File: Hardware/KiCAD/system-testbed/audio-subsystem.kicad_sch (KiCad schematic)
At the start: 29 parts, among them J1 Conn_02x13_Odd_Even, SW1 SW_SPDT, U2 MAX98357A

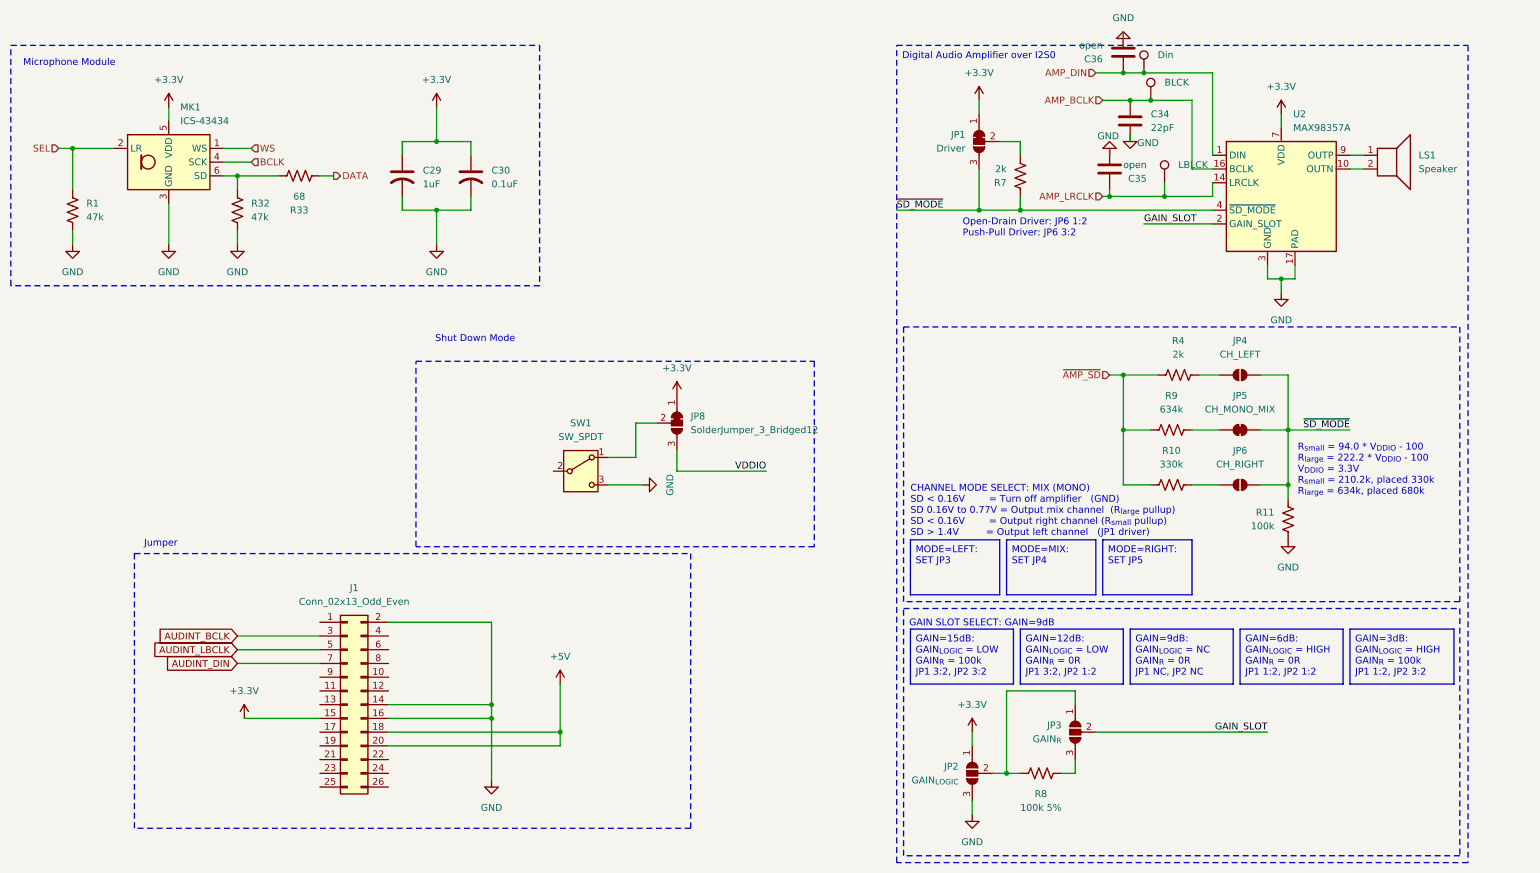
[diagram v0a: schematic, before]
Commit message: feat: capture Audio PCB #32 feat: begin I2S Pin Mapping and Interconnects #53
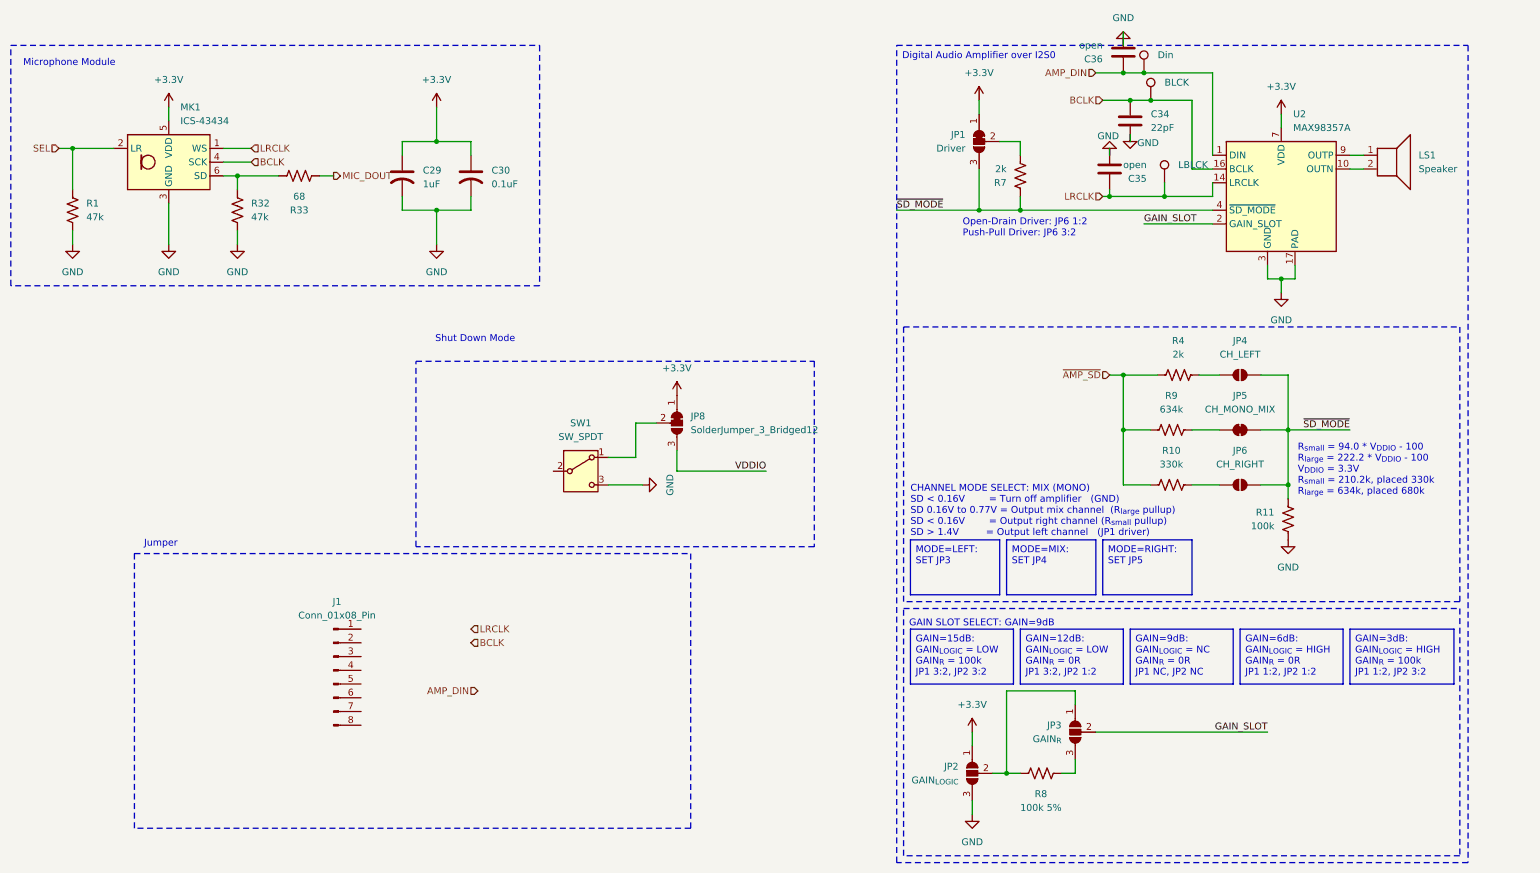
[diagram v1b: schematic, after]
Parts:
- J1: value Conn_02x13_Odd_Even -> Conn_01x08_Pin; symbol Connector_Generic:Conn_02x13_Odd_Even -> Connector:Conn_01x08_Pin
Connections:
- net AMP_BCLK is gone; now on net BCLK: BLCK.1, C34.1, U2.16 (BCLK)
- net WS is gone; now on net LRCLK: MK1.1 (WS)
- net +3.3V: no longer J1.15 (Pin_15)
- net GND: no longer J1.14 (Pin_14), J1.16 (Pin_16), J1.2 (Pin_2)
- removed net +5V: J1.18 (Pin_18), J1.20 (Pin_20)
- net AMP_LRCLK renamed LRCLK
- net AUDINT_BCLK: no longer names the net of J1.3 (Pin_3)
- net AUDINT_DIN: no longer names the net of J1.7 (Pin_7)
- net AUDINT_LBCLK: no longer names the net of J1.5 (Pin_5)
- net DATA renamed MIC_DOUT

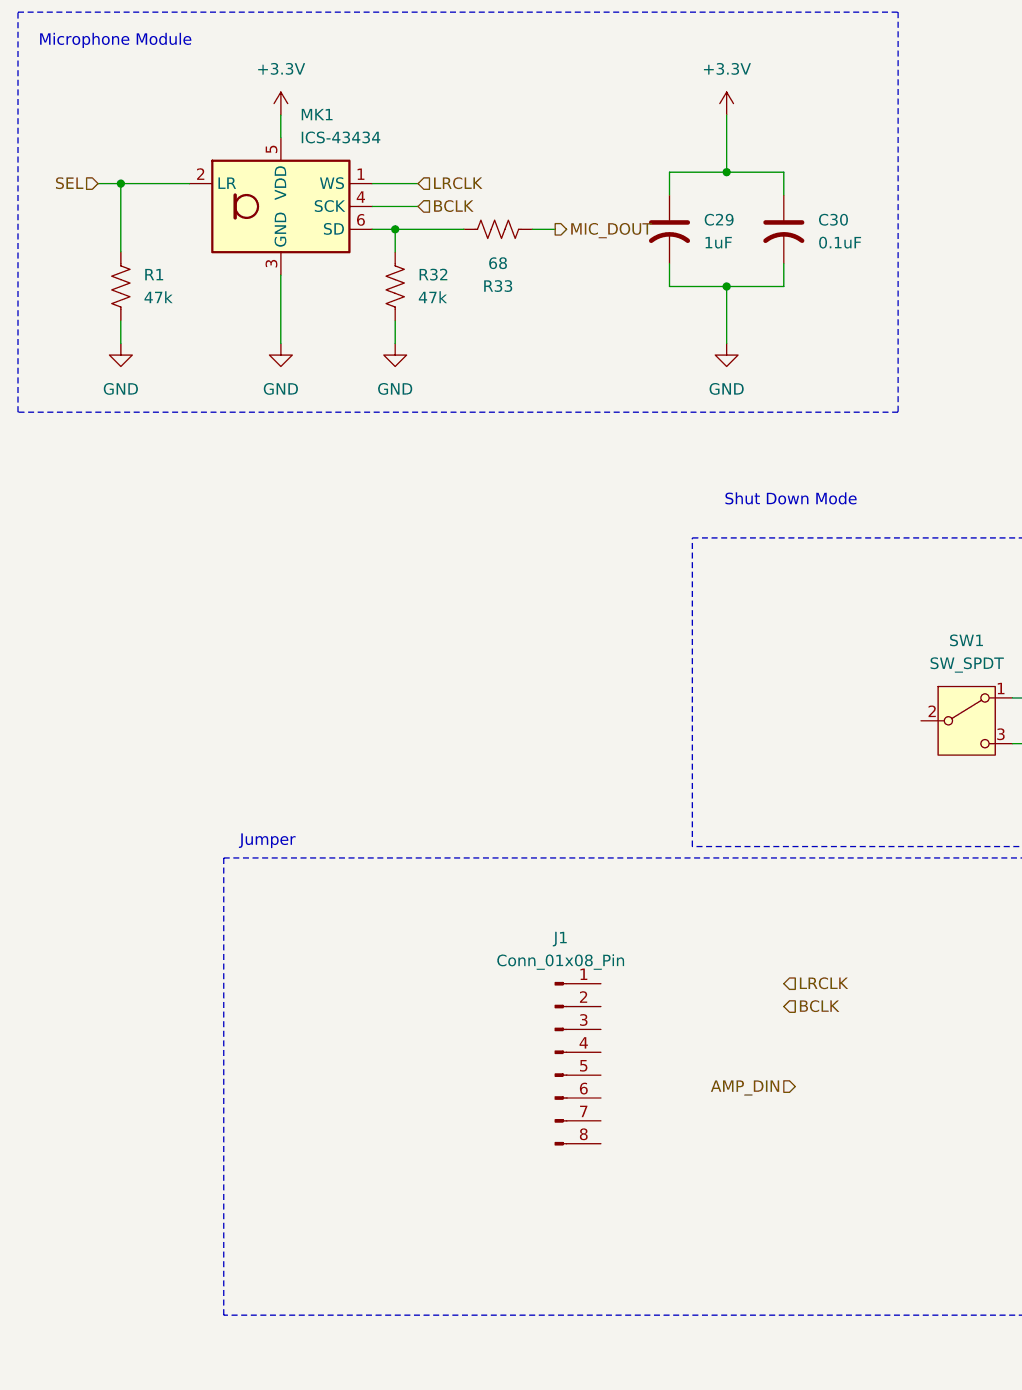
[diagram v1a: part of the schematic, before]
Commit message: fix: clarify labellng and pin head #32
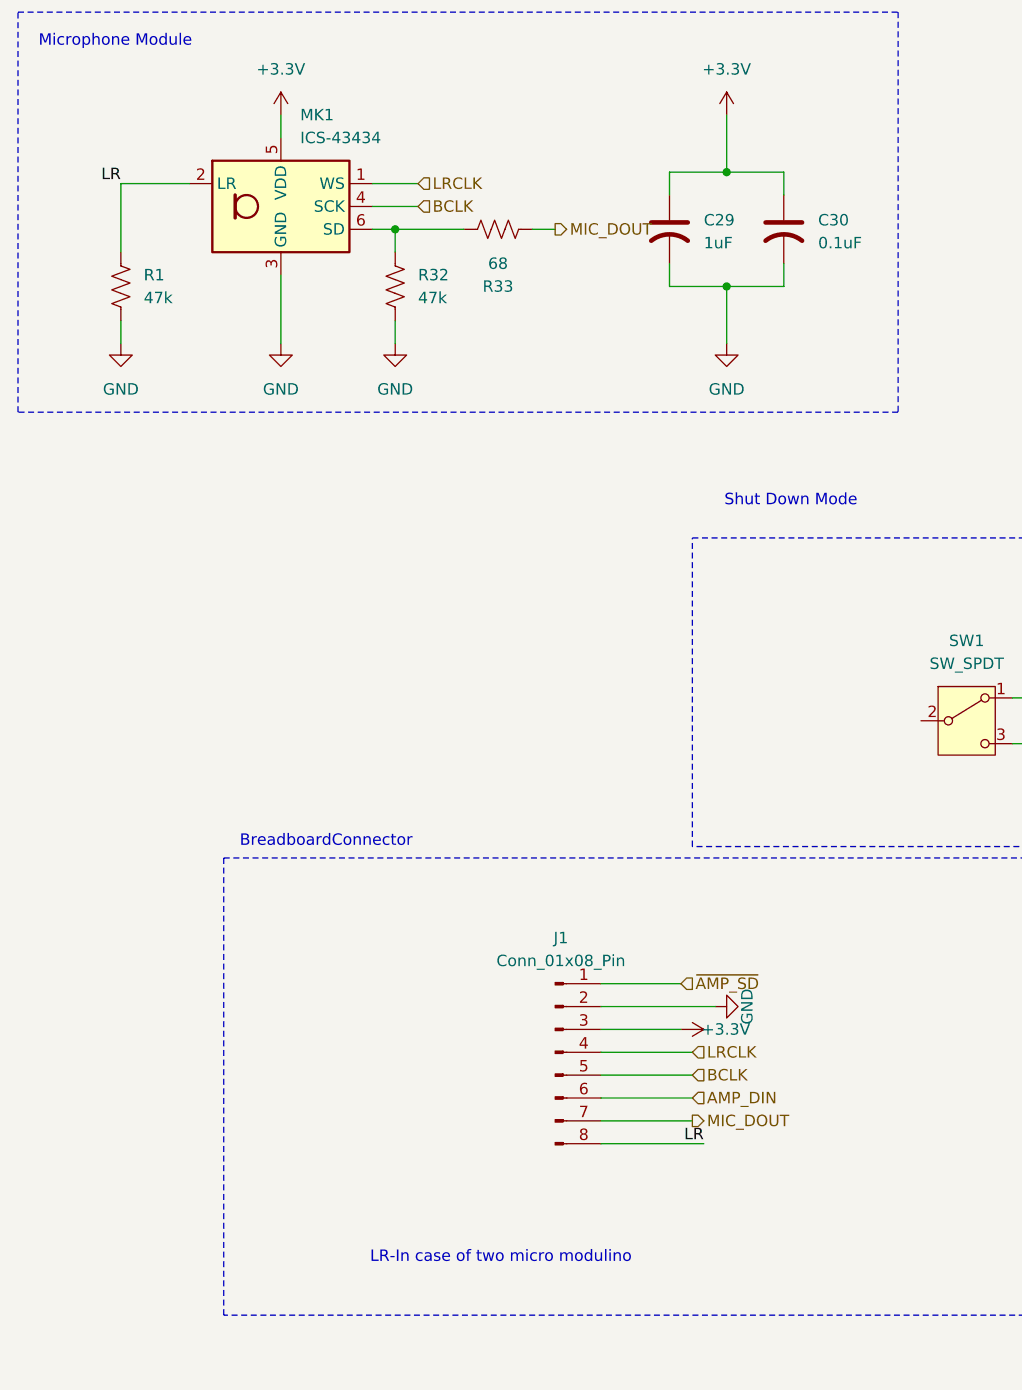
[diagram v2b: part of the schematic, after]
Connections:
- net SEL is gone; now on net LR: MK1.2 (LR), R1.1
- net +3.3V: now also J1.3 (Pin_3)
- net AMP_DIN: now also J1.6 (Pin_6)
- net BCLK: now also J1.5 (Pin_5)
- net GND: now also J1.2 (Pin_2)
- net LRCLK: now also J1.4 (Pin_4)
- net MIC_DOUT: now also J1.7 (Pin_7)
- net ~{AMP_SD}: now also J1.1 (Pin_1)
- net LR: now reaches J1.8 (Pin_8)
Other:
- note added: "BreadboardConnector"
- note added: "LR-In case of two micro modulino"
- note removed: "Jumper"

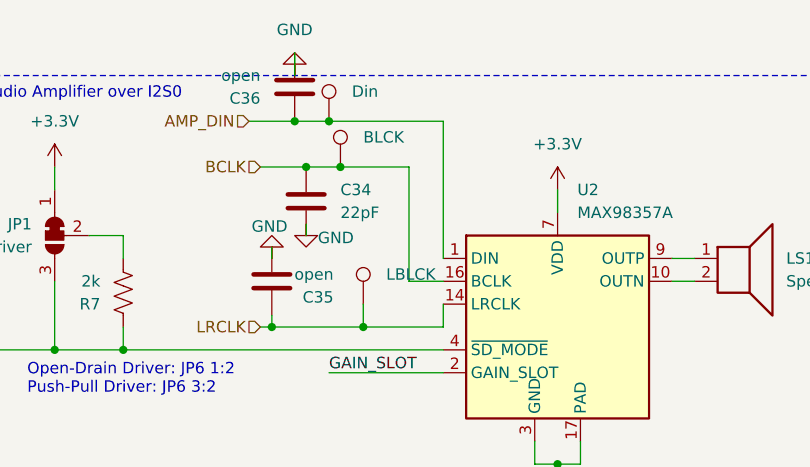
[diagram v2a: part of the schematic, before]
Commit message: fix: begin reannotations #65 #70
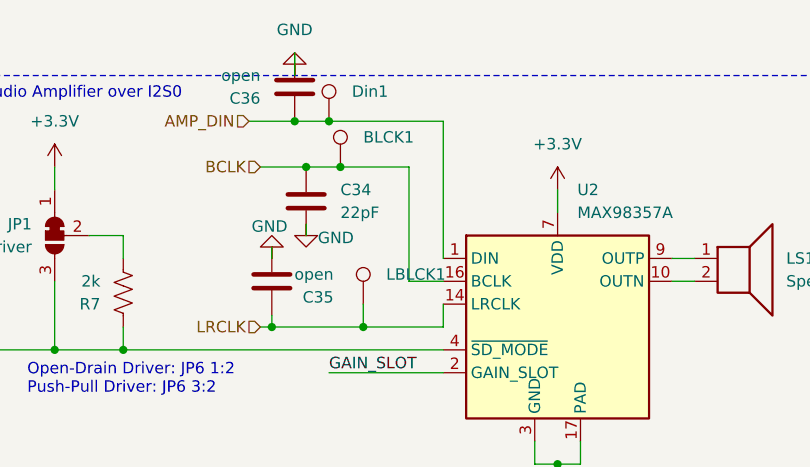
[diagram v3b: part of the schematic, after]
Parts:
- renumbered BLCK to BLCK1, Din to Din1, LBLCK to LBLCK1
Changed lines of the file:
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@@
 		(dnp no)
 		(fields_autoplaced yes)
-		(property "Reference" "#PWR05"
+		(property "Reference" "#PWR0104"
 			(at 248.92 66.04 0)
 			(effects
@@
 			(project "system-testbed"
 				(path "/72756aea-0ff9-4757-9699-8d0f18588f6f/d4290985-9747-4b26-ad72-a8210ee01731"
-					(reference "#PWR05")
+					(reference "#PWR0104")
 					(unit 1)
 				)
@@
 		(on_board yes)
 		(dnp no)
-		(property "Reference" "#PWR02"
+		(property "Reference" "#PWR0106"
 			(at 43.18 57.15 0)
 			(effects
@@
 			(project "system-testbed"
 				(path "/72756aea-0ff9-4757-9699-8d0f18588f6f/d4290985-9747-4b26-ad72-a8210ee01731"
-					(reference "#PWR02")
+					(reference "#PWR0106")
 					(unit 1)
 				)
@@
 		(dnp no)
 		(fields_autoplaced yes)
-		(property "Reference" "#PWR01"
+		(property "Reference" "#PWR0107"
 			(at 43.18 29.21 0)
 			(effects
@@
 			(project "system-testbed"
 				(path "/72756aea-0ff9-4757-9699-8d0f18588f6f/d4290985-9747-4b26-ad72-a8210ee01731"
-					(reference "#PWR01")
+					(reference "#PWR0107")
 					(unit 1)
 				)
@@
 		(dnp no)
 		(fields_autoplaced yes)
-		(property "Reference" "#PWR03"
+		(property "Reference" "#PWR0105"
 			(at 25.4 57.15 0)
 			(effects
@@
 			(project "system-testbed"
 				(path "/72756aea-0ff9-4757-9699-8d0f18588f6f/d4290985-9747-4b26-ad72-a8210ee01731"
-					(reference "#PWR03")
+					(reference "#PWR0105")
 					(unit 1)
 				)
@@
 		(dnp no)
 		(fields_autoplaced yes)
-		(property "Reference" "BLCK"
+		(property "Reference" "BLCK1"
 			(at 227.33 20.8279 0)
 			(effects
@@
 			(project "system-testbed"
 				(path "/72756aea-0ff9-4757-9699-8d0f18588f6f/d4290985-9747-4b26-ad72-a8210ee01731"
-					(reference "BLCK")
+					(reference "BLCK1")
 					(unit 1)
 				)
@@
 		(dnp no)
 		(fields_autoplaced yes)
-		(property "Reference" "LBLCK"
+		(property "Reference" "LBLCK1"
 			(at 229.87 36.0679 0)
 			(effects
@@
 			(project "system-testbed"
 				(path "/72756aea-0ff9-4757-9699-8d0f18588f6f/d4290985-9747-4b26-ad72-a8210ee01731"
-					(reference "LBLCK")
+					(reference "LBLCK1")
 					(unit 1)
 				)
@@
 		(dnp no)
 		(fields_autoplaced yes)
-		(property "Reference" "Din"
+		(property "Reference" "Din1"
 			(at 226.06 15.7479 0)
 			(effects
@@
 			(project ""
 				(path "/72756aea-0ff9-4757-9699-8d0f18588f6f/d4290985-9747-4b26-ad72-a8210ee01731"
-					(reference "Din")
+					(reference "Din1")
 					(unit 1)
 				)

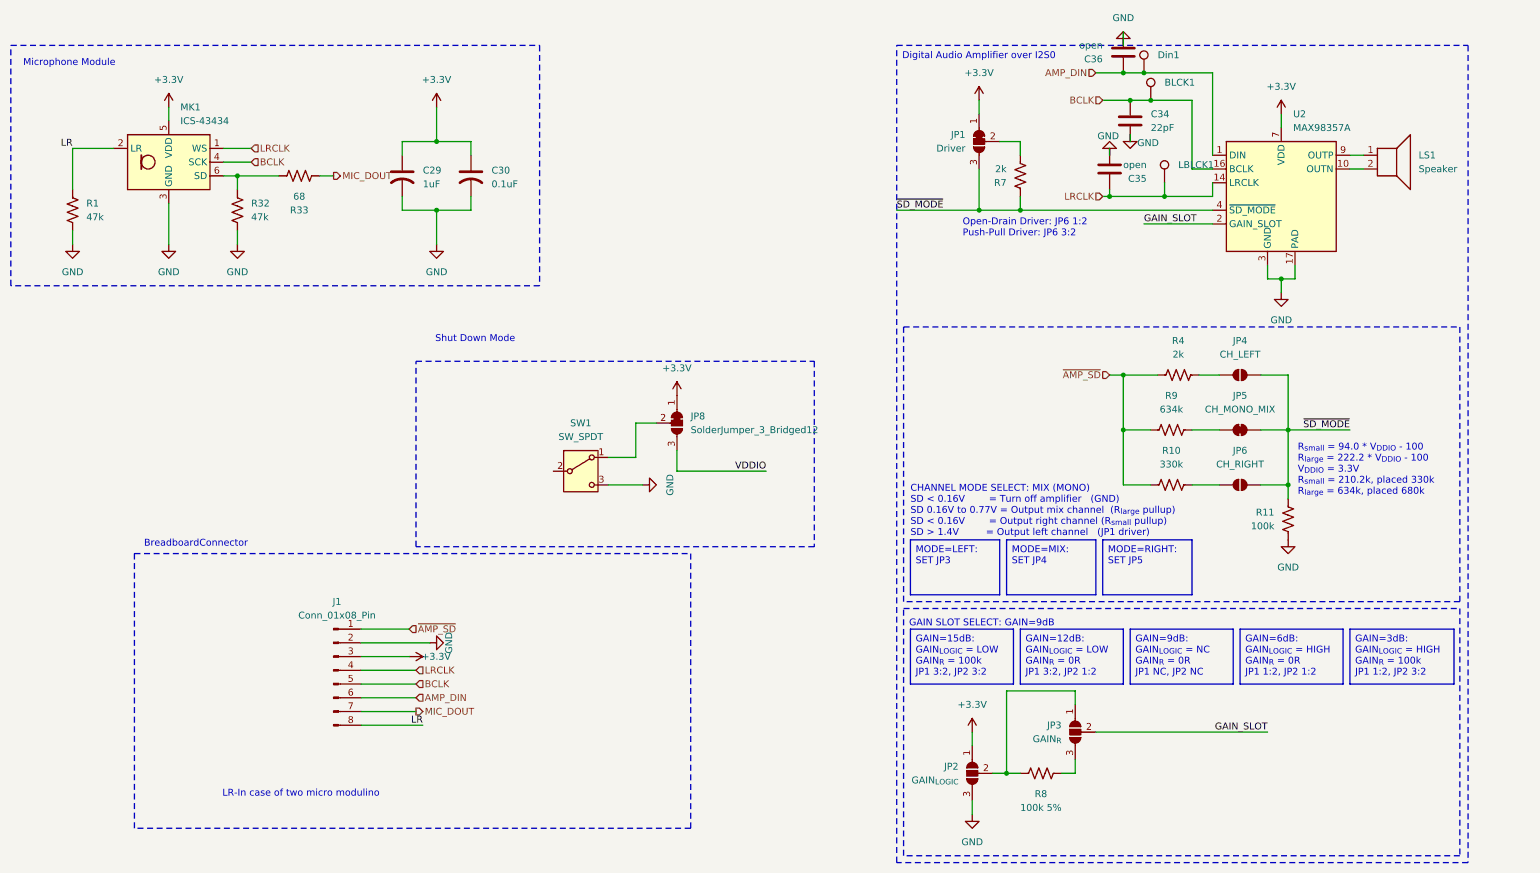
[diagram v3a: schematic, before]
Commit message: fix: reannotate schematics for pcb editor use #55
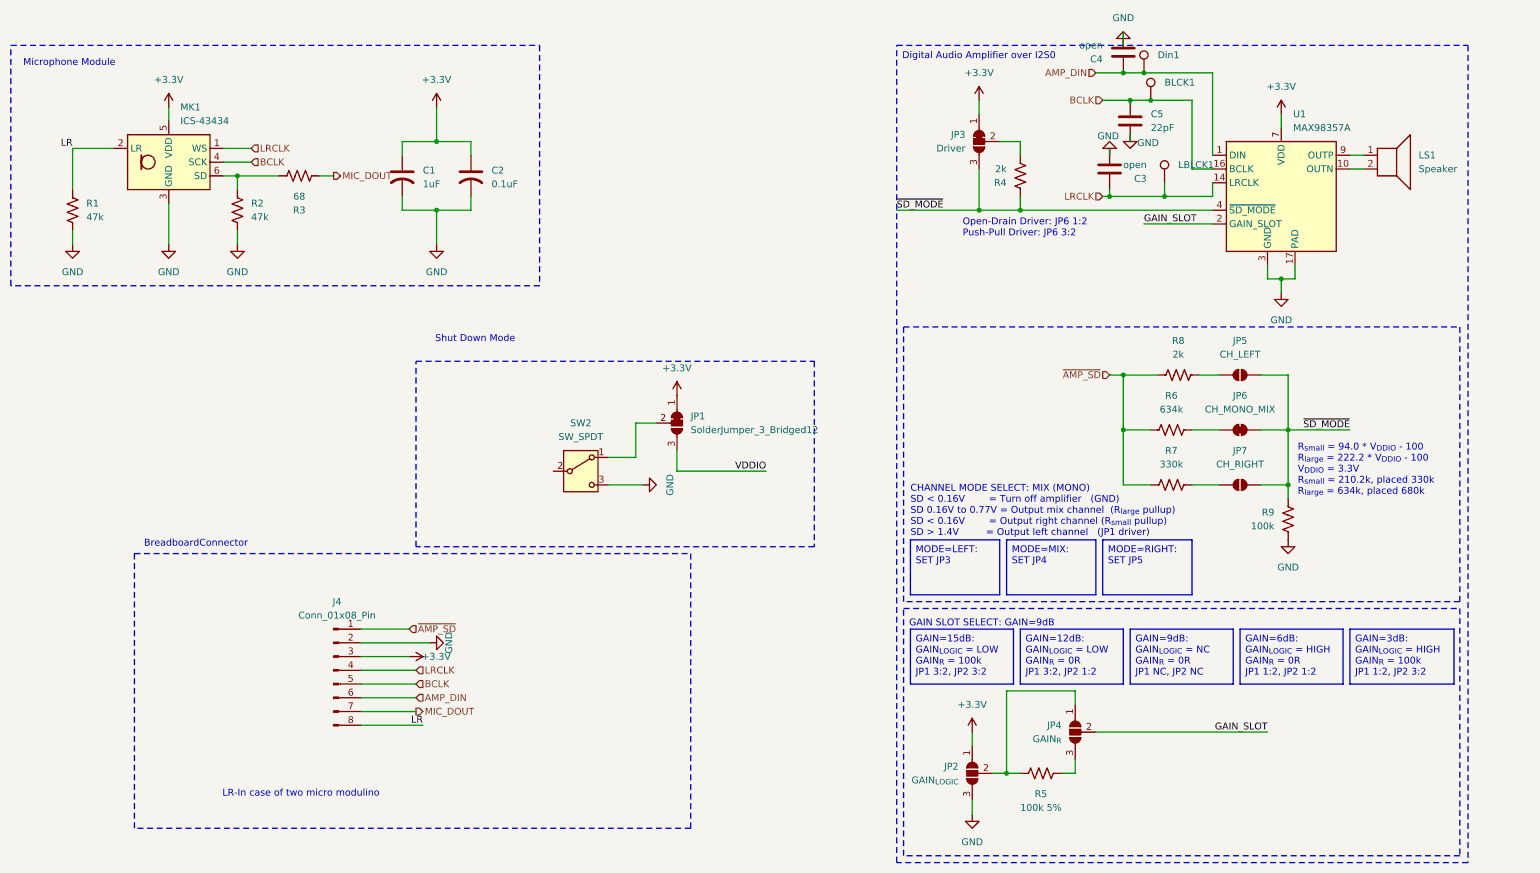
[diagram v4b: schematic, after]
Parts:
- C5: renamed from C34; footprint (none) -> Capacitor_SMD:C_0603_1608Metric
- renumbered C29 to C1, C30 to C2, C35 to C3, C36 to C4, J1 to J4, JP8 to JP1, JP1 to JP3, JP3 to JP4, JP4 to JP5, JP5 to JP6, JP6 to JP7, R32 to R2, R33 to R3, R7 to R4, R8 to R5, R9 to R6, R10 to R7, R4 to R8, R11 to R9, SW1 to SW2, U2 to U1
